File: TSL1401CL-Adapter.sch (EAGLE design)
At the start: 3 parts

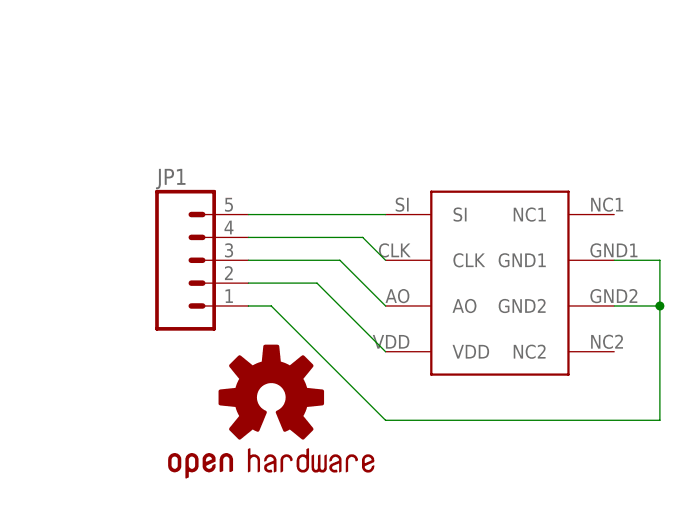
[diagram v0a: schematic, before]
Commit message: Added 2x3 Shroud and made the board square with drill holes
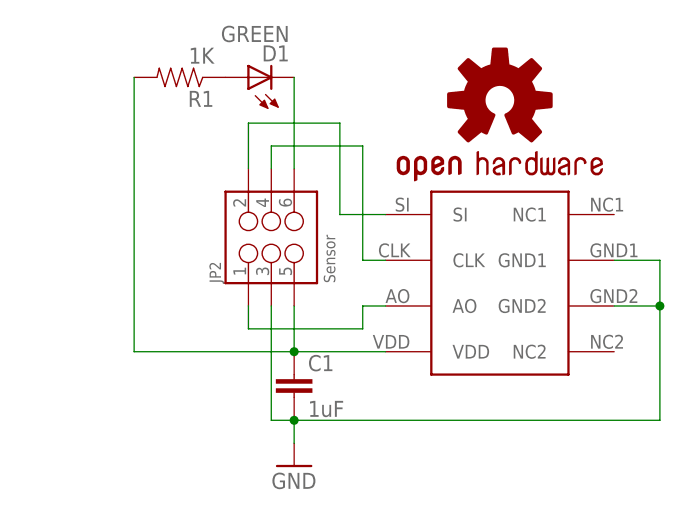
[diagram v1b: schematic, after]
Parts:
- removed JP1: (no value), SparkFun:M05LOCK_LONGPADS
- added C1: 1uF, SparkFun-Passives:CAP0603-CAP
- added D1: GREEN, SparkFun-LED:LED-GREEN0603
- added JP2: Sensor, SparkFun-Connectors:M03X2
- added R1: 1K, SparkFun-Resistors:RESISTOR0603-RES
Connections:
- new net GND: C1.2, JP2.3, U$1.GND1, U$1.GND2
- new net N$6: D1.C, JP2.6
- net N$1: now also JP2.2; no longer JP1.5
- net N$2: now also JP2.4; no longer JP1.4
- net N$3: now also JP2.1; no longer JP1.3
- net N$4: now also C1.1, JP2.5, R1.2; no longer JP1.2
- net N$5: now also D1.A, R1.1; no longer JP1.1, U$1.GND1, U$1.GND2
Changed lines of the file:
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@@
 <layer number="144" name="Drill_legend" color="7" fill="1" visible="no" active="yes"/>
 <layer number="151" name="HeatSink" color="7" fill="1" visible="no" active="yes"/>
+<layer number="199" name="Contour" color="7" fill="1" visible="yes" active="yes"/>
 <layer number="200" name="200bmp" color="1" fill="10" visible="no" active="yes"/>
 <layer number="201" name="201bmp" color="2" fill="10" visible="no" active="yes"/>
@@
 <parts>
 <part name="U$1" library="BIG" deviceset="TSL1401" device="CL"/>
-<part name="JP1" library="SparkFun" deviceset="M05" device="LOCK_LONGPADS"/>
 <part name="U$2" library="SparkFun" deviceset="OSHW-LOGO" device="M"/>
+<part name="JP2" library="SparkFun-Connectors" deviceset="M03X2" device="" value="Sensor"/>
+<part name="C1" library="SparkFun-Passives" deviceset="CAP" device="0603-CAP" value="1uF"/>
+<part name="GND1" library="SparkFun-Aesthetics" deviceset="GND" device=""/>
+<part name="R1" library="SparkFun-Resistors" deviceset="RESISTOR" device="0603-RES" value="1K"/>
+<part name="D1" library="SparkFun-LED" deviceset="LED-GREEN" device="0603" value="GREEN"/>
 </parts>
 <sheets>
@@
 <instances>
 <instance part="U$1" gate="G$1" x="78.74" y="50.8"/>
-<instance part="JP1" gate="G$1" x="43.18" y="53.34"/>
-<instance part="U$2" gate="G$1" x="53.34" y="38.1"/>
+<instance part="U$2" gate="G$1" x="78.74" y="71.12"/>
+<instance part="JP2" gate="G$1" x="53.34" y="55.88" smashed="yes" rot="R90">
+<attribute name="NAME" x="47.752" y="50.8" size="1.27" layer="95" rot="R90"/>
+<attribute name="VALUE" x="60.452" y="50.8" size="1.27" layer="96" rot="R90"/>
+</instance>
+<instance part="C1" gate="G$1" x="55.88" y="38.1"/>
+<instance part="GND1" gate="1" x="55.88" y="30.48"/>
+<instance part="R1" gate="G$1" x="43.18" y="73.66" rot="R180"/>
+<instance part="D1" gate="G$1" x="50.8" y="73.66" rot="R90"/>
 </instances>
 <busses>
@@
 <net name="N$1" class="0">
 <segment>
-<wire x1="66.04" y1="58.42" x2="50.8" y2="58.42" width="0.1524" layer="91"/>
+<wire x1="66.04" y1="58.42" x2="60.96" y2="58.42" width="0.1524" layer="91"/>
 <pinref part="U$1" gate="G$1" pin="SI"/>
-<pinref part="JP1" gate="G$1" pin="5"/>
+<wire x1="60.96" y1="58.42" x2="60.96" y2="68.58" width="0.1524" layer="91"/>
+<wire x1="60.96" y1="68.58" x2="50.8" y2="68.58" width="0.1524" layer="91"/>
+<pinref part="JP2" gate="G$1" pin="2"/>
+<wire x1="50.8" y1="68.58" x2="50.8" y2="63.5" width="0.1524" layer="91"/>
 </segment>
 </net>
 <net name="N$2" class="0">
 <segment>
-<wire x1="66.04" y1="53.34" x2="63.5" y2="55.88" width="0.1524" layer="91"/>
-<wire x1="63.5" y1="55.88" x2="50.8" y2="55.88" width="0.1524" layer="91"/>
+<wire x1="66.04" y1="53.34" x2="63.5" y2="53.34" width="0.1524" layer="91"/>
+<wire x1="63.5" y1="53.34" x2="63.5" y2="66.04" width="0.1524" layer="91"/>
 <pinref part="U$1" gate="G$1" pin="CLK"/>
-<pinref part="JP1" gate="G$1" pin="4"/>
+<wire x1="63.5" y1="66.04" x2="53.34" y2="66.04" width="0.1524" layer="91"/>
+<pinref part="JP2" gate="G$1" pin="4"/>
+<wire x1="53.34" y1="66.04" x2="53.34" y2="63.5" width="0.1524" layer="91"/>
 </segment>
 </net>
 <net name="N$3" class="0">
 <segment>
-<wire x1="66.04" y1="48.26" x2="60.96" y2="53.34" width="0.1524" layer="91"/>
-<wire x1="60.96" y1="53.34" x2="50.8" y2="53.34" width="0.1524" layer="91"/>
+<wire x1="66.04" y1="48.26" x2="63.5" y2="48.26" width="0.1524" layer="91"/>
+<wire x1="63.5" y1="48.26" x2="63.5" y2="45.72" width="0.1524" layer="91"/>
+<wire x1="63.5" y1="45.72" x2="50.8" y2="45.72" width="0.1524" layer="91"/>
+<wire x1="50.8" y1="45.72" x2="50.8" y2="48.26" width="0.1524" layer="91"/>
 <pinref part="U$1" gate="G$1" pin="AO"/>
-<pinref part="JP1" gate="G$1" pin="3"/>
+<pinref part="JP2" gate="G$1" pin="1"/>
 </segment>
 </net>
 <net name="N$4" class="0">
 <segment>
-<wire x1="66.04" y1="43.18" x2="58.42" y2="50.8" width="0.1524" layer="91"/>
-<wire x1="58.42" y1="50.8" x2="50.8" y2="50.8" width="0.1524" layer="91"/>
+<wire x1="66.04" y1="43.18" x2="55.88" y2="43.18" width="0.1524" layer="91"/>
+<wire x1="55.88" y1="43.18" x2="55.88" y2="48.26" width="0.1524" layer="91"/>
 <pinref part="U$1" gate="G$1" pin="VDD"/>
-<pinref part="JP1" gate="G$1" pin="2"/>
+<pinref part="JP2" gate="G$1" pin="5"/>
+<pinref part="C1" gate="G$1" pin="1"/>
+<junction x="55.88" y="43.18"/>
+<wire x1="55.88" y1="43.18" x2="38.1" y2="43.18" width="0.1524" layer="91"/>
+<wire x1="38.1" y1="43.18" x2="38.1" y2="73.66" width="0.1524" layer="91"/>
+<pinref part="R1" gate="G$1" pin="2"/>
+</segment>
+</net>
+<net name="GND" class="0">
+<segment>
+<pinref part="C1" gate="G$1" pin="2"/>
+<pinref part="GND1" gate="1" pin="GND"/>
+<wire x1="55.88" y1="33.02" x2="55.88" y2="35.56" width="0.1524" layer="91"/>
+<pinref part="U$1" gate="G$1" pin="GND1"/>
+<wire x1="91.44" y1="53.34" x2="96.52" y2="53.34" width="0.1524" layer="91"/>
+<wire x1="96.52" y1="53.34" x2="96.52" y2="48.26" width="0.1524" layer="91"/>
+<wire x1="91.44" y1="48.26" x2="96.52" y2="48.26" width="0.1524" layer="91"/>
+<pinref part="U$1" gate="G$1" pin="GND2"/>
+<wire x1="96.52" y1="48.26" x2="96.52" y2="35.56" width="0.1524" layer="91"/>
+<junction x="96.52" y="48.26"/>
+<wire x1="53.34" y1="35.56" x2="53.34" y2="48.26" width="0.1524" layer="91"/>
+<pinref part="JP2" gate="G$1" pin="3"/>
+<wire x1="96.52" y1="35.56" x2="55.88" y2="35.56" width="0.1524" layer="91"/>
+<junction x="55.88" y="35.56"/>
+<wire x1="55.88" y1="35.56" x2="53.34" y2="35.56" width="0.1524" layer="91"/>
 </segment>
 </net>
 <net name="N$5" class="0">
 <segment>
-<wire x1="91.44" y1="53.34" x2="96.52" y2="53.34" width="0.1524" layer="91"/>
-<wire x1="96.52" y1="53.34" x2="96.52" y2="48.26" width="0.1524" layer="91"/>
-<wire x1="96.52" y1="48.26" x2="96.52" y2="35.56" width="0.1524" layer="91"/>
-<wire x1="96.52" y1="35.56" x2="66.04" y2="35.56" width="0.1524" layer="91"/>
-<wire x1="66.04" y1="35.56" x2="53.34" y2="48.26" width="0.1524" layer="91"/>
-<wire x1="53.34" y1="48.26" x2="50.8" y2="48.26" width="0.1524" layer="91"/>
-<wire x1="91.44" y1="48.26" x2="96.52" y2="48.26" width="0.1524" layer="91"/>
-<junction x="96.52" y="48.26"/>
-<pinref part="U$1" gate="G$1" pin="GND1"/>
-<pinref part="JP1" gate="G$1" pin="1"/>
-<pinref part="U$1" gate="G$1" pin="GND2"/>
+<pinref part="R1" gate="G$1" pin="1"/>
+<pinref part="D1" gate="G$1" pin="A"/>
 </segment>
 </net>
+<net name="N$6" class="0">
+<segment>
+<pinref part="D1" gate="G$1" pin="C"/>
+<pinref part="JP2" gate="G$1" pin="6"/>
+<wire x1="55.88" y1="73.66" x2="55.88" y2="63.5" width="0.1524" layer="91"/>
+</segment>
+</net>

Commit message: Modified to be used as a remote sensor to the pgFocus project
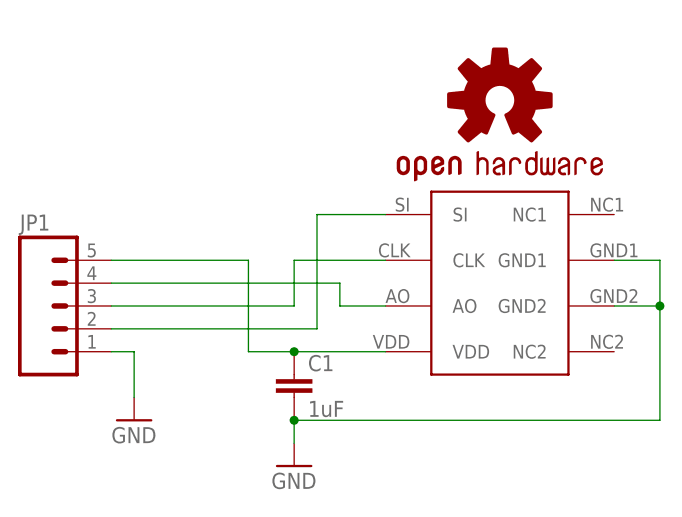
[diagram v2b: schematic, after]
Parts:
- removed D1: GREEN, SparkFun-LED:LED-GREEN0603
- removed JP2: Sensor, SparkFun-Connectors:M03X2
- removed R1: 1K, SparkFun-Resistors:RESISTOR0603-RES
- added JP1: (no value), SparkFun-Connectors:M05LOCK
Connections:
- removed net N$1: JP2.2, U$1.SI
- removed net N$2: JP2.4, U$1.CLK
- removed net N$3: JP2.1, U$1.AO
- removed net N$4: C1.1, JP2.5, R1.2, U$1.VDD
- removed net N$5: D1.A, R1.1
- removed net N$6: D1.C, JP2.6
- new net +5V: C1.1, JP1.5, U$1.VDD
- new net AO: JP1.4, U$1.AO
- new net CLK: JP1.3, U$1.CLK
- new net SI: JP1.2, U$1.SI
- net GND: now also JP1.1; no longer JP2.3
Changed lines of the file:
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@@
 <part name="U$1" library="BIG" deviceset="TSL1401" device="CL"/>
 <part name="U$2" library="SparkFun" deviceset="OSHW-LOGO" device="M"/>
-<part name="JP2" library="SparkFun-Connectors" deviceset="M03X2" device="" value="Sensor"/>
 <part name="C1" library="SparkFun-Passives" deviceset="CAP" device="0603-CAP" value="1uF"/>
 <part name="GND1" library="SparkFun-Aesthetics" deviceset="GND" device=""/>
-<part name="R1" library="SparkFun-Resistors" deviceset="RESISTOR" device="0603-RES" value="1K"/>
-<part name="D1" library="SparkFun-LED" deviceset="LED-GREEN" device="0603" value="GREEN"/>
+<part name="JP1" library="SparkFun-Connectors" deviceset="M05" device="LOCK"/>
+<part name="GND2" library="SparkFun-Aesthetics" deviceset="GND" device=""/>
 </parts>
 <sheets>
@@
 <instance part="U$1" gate="G$1" x="78.74" y="50.8"/>
 <instance part="U$2" gate="G$1" x="78.74" y="71.12"/>
-<instance part="JP2" gate="G$1" x="53.34" y="55.88" smashed="yes" rot="R90">
-<attribute name="NAME" x="47.752" y="50.8" size="1.27" layer="95" rot="R90"/>
-<attribute name="VALUE" x="60.452" y="50.8" size="1.27" layer="96" rot="R90"/>
-</instance>
 <instance part="C1" gate="G$1" x="55.88" y="38.1"/>
 <instance part="GND1" gate="1" x="55.88" y="30.48"/>
-<instance part="R1" gate="G$1" x="43.18" y="73.66" rot="R180"/>
-<instance part="D1" gate="G$1" x="50.8" y="73.66" rot="R90"/>
+<instance part="JP1" gate="G$1" x="27.94" y="48.26"/>
+<instance part="GND2" gate="1" x="38.1" y="35.56"/>
 </instances>
 <busses>
 </busses>
 <nets>
-<net name="N$1" class="0">
-<segment>
-<wire x1="66.04" y1="58.42" x2="60.96" y2="58.42" width="0.1524" layer="91"/>
-<pinref part="U$1" gate="G$1" pin="SI"/>
-<wire x1="60.96" y1="58.42" x2="60.96" y2="68.58" width="0.1524" layer="91"/>
-<wire x1="60.96" y1="68.58" x2="50.8" y2="68.58" width="0.1524" layer="91"/>
-<pinref part="JP2" gate="G$1" pin="2"/>
-<wire x1="50.8" y1="68.58" x2="50.8" y2="63.5" width="0.1524" layer="91"/>
-</segment>
-</net>
-<net name="N$2" class="0">
-<segment>
-<wire x1="66.04" y1="53.34" x2="63.5" y2="53.34" width="0.1524" layer="91"/>
-<wire x1="63.5" y1="53.34" x2="63.5" y2="66.04" width="0.1524" layer="91"/>
-<pinref part="U$1" gate="G$1" pin="CLK"/>
-<wire x1="63.5" y1="66.04" x2="53.34" y2="66.04" width="0.1524" layer="91"/>
-<pinref part="JP2" gate="G$1" pin="4"/>
-<wire x1="53.34" y1="66.04" x2="53.34" y2="63.5" width="0.1524" layer="91"/>
-</segment>
-</net>
-<net name="N$3" class="0">
-<segment>
-<wire x1="66.04" y1="48.26" x2="63.5" y2="48.26" width="0.1524" layer="91"/>
-<wire x1="63.5" y1="48.26" x2="63.5" y2="45.72" width="0.1524" layer="91"/>
-<wire x1="63.5" y1="45.72" x2="50.8" y2="45.72" width="0.1524" layer="91"/>
-<wire x1="50.8" y1="45.72" x2="50.8" y2="48.26" width="0.1524" layer="91"/>
-<pinref part="U$1" gate="G$1" pin="AO"/>
-<pinref part="JP2" gate="G$1" pin="1"/>
-</segment>
-</net>
-<net name="N$4" class="0">
+<net name="+5V" class="0">
 <segment>
 <wire x1="66.04" y1="43.18" x2="55.88" y2="43.18" width="0.1524" layer="91"/>
-<wire x1="55.88" y1="43.18" x2="55.88" y2="48.26" width="0.1524" layer="91"/>
 <pinref part="U$1" gate="G$1" pin="VDD"/>
-<pinref part="JP2" gate="G$1" pin="5"/>
 <pinref part="C1" gate="G$1" pin="1"/>
+<wire x1="55.88" y1="43.18" x2="50.8" y2="43.18" width="0.1524" layer="91"/>
 <junction x="55.88" y="43.18"/>
-<wire x1="55.88" y1="43.18" x2="38.1" y2="43.18" width="0.1524" layer="91"/>
-<wire x1="38.1" y1="43.18" x2="38.1" y2="73.66" width="0.1524" layer="91"/>
-<pinref part="R1" gate="G$1" pin="2"/>
+<wire x1="50.8" y1="43.18" x2="50.8" y2="53.34" width="0.1524" layer="91"/>
+<pinref part="JP1" gate="G$1" pin="5"/>
+<wire x1="50.8" y1="53.34" x2="35.56" y2="53.34" width="0.1524" layer="91"/>
 </segment>
 </net>
@@
 <wire x1="96.52" y1="48.26" x2="96.52" y2="35.56" width="0.1524" layer="91"/>
 <junction x="96.52" y="48.26"/>
-<wire x1="53.34" y1="35.56" x2="53.34" y2="48.26" width="0.1524" layer="91"/>
-<pinref part="JP2" gate="G$1" pin="3"/>
 <wire x1="96.52" y1="35.56" x2="55.88" y2="35.56" width="0.1524" layer="91"/>
 <junction x="55.88" y="35.56"/>
-<wire x1="55.88" y1="35.56" x2="53.34" y2="35.56" width="0.1524" layer="91"/>
+</segment>
+<segment>
+<pinref part="GND2" gate="1" pin="GND"/>
+<wire x1="38.1" y1="38.1" x2="38.1" y2="43.18" width="0.1524" layer="91"/>
+<pinref part="JP1" gate="G$1" pin="1"/>
+<wire x1="38.1" y1="43.18" x2="35.56" y2="43.18" width="0.1524" layer="91"/>
 </segment>
 </net>
-<net name="N$5" class="0">
+<net name="SI" class="0">
 <segment>
-<pinref part="R1" gate="G$1" pin="1"/>
-<pinref part="D1" gate="G$1" pin="A"/>
+<pinref part="U$1" gate="G$1" pin="SI"/>
+<wire x1="66.04" y1="58.42" x2="58.42" y2="58.42" width="0.1524" layer="91"/>
+<wire x1="58.42" y1="58.42" x2="58.42" y2="45.72" width="0.1524" layer="91"/>
+<pinref part="JP1" gate="G$1" pin="2"/>
+<wire x1="58.42" y1="45.72" x2="35.56" y2="45.72" width="0.1524" layer="91"/>
 </segment>
 </net>
-<net name="N$6" class="0">
+<net name="AO" class="0">
 <segment>
-<pinref part="D1" gate="G$1" pin="C"/>
-<pinref part="JP2" gate="G$1" pin="6"/>
-<wire x1="55.88" y1="73.66" x2="55.88" y2="63.5" width="0.1524" layer="91"/>
+<pinref part="U$1" gate="G$1" pin="AO"/>
+<wire x1="66.04" y1="48.26" x2="60.96" y2="48.26" width="0.1524" layer="91"/>
+<wire x1="60.96" y1="48.26" x2="60.96" y2="50.8" width="0.1524" layer="91"/>
+<pinref part="JP1" gate="G$1" pin="4"/>
+<wire x1="60.96" y1="50.8" x2="35.56" y2="50.8" width="0.1524" layer="91"/>
 </segment>
 </net>
+<net name="CLK" class="0">
+<segment>
+<pinref part="U$1" gate="G$1" pin="CLK"/>
+<wire x1="66.04" y1="53.34" x2="55.88" y2="53.34" width="0.1524" layer="91"/>
+<wire x1="55.88" y1="53.34" x2="55.88" y2="48.26" width="0.1524" layer="91"/>
+<pinref part="JP1" gate="G$1" pin="3"/>
+<wire x1="55.88" y1="48.26" x2="35.56" y2="48.26" width="0.1524" layer="91"/>
+</segment>
+</net>

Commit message: Changed connector to JST 5 Pin
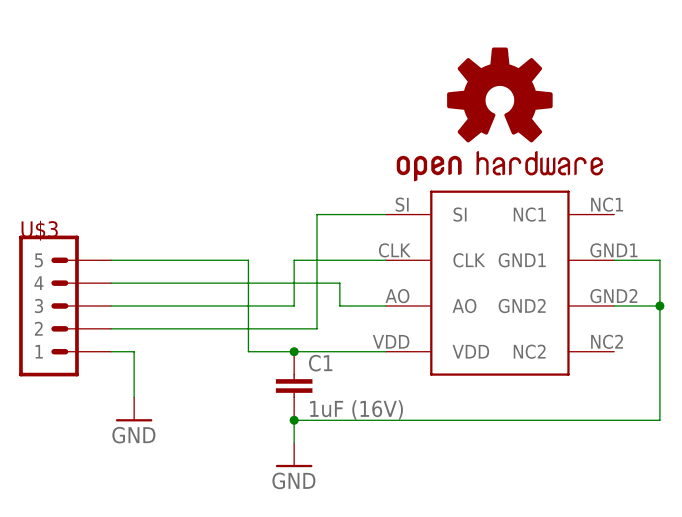
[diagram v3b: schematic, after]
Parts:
- removed JP1: (no value), SparkFun-Connectors:M05LOCK
- added U$3: M05, BIG:M05
- C1: value 1uF -> 1uF (16V)
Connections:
- net +5V: now also U$3.5; no longer JP1.5
- net AO: now also U$3.4; no longer JP1.4
- net CLK: now also U$3.3; no longer JP1.3
- net GND: now also U$3.1; no longer JP1.1
- net SI: now also U$3.2; no longer JP1.2
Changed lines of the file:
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@@
 <part name="U$1" library="BIG" deviceset="TSL1401" device="CL"/>
 <part name="U$2" library="SparkFun" deviceset="OSHW-LOGO" device="M"/>
-<part name="C1" library="SparkFun-Passives" deviceset="CAP" device="0603-CAP" value="1uF"/>
+<part name="C1" library="SparkFun-Passives" deviceset="CAP" device="0603-CAP" value="1uF (16V)"/>
 <part name="GND1" library="SparkFun-Aesthetics" deviceset="GND" device=""/>
-<part name="JP1" library="SparkFun-Connectors" deviceset="M05" device="LOCK"/>
 <part name="GND2" library="SparkFun-Aesthetics" deviceset="GND" device=""/>
+<part name="U$3" library="BIG" deviceset="M05" device=""/>
 </parts>
 <sheets>
@@
 <instance part="C1" gate="G$1" x="55.88" y="38.1"/>
 <instance part="GND1" gate="1" x="55.88" y="30.48"/>
-<instance part="JP1" gate="G$1" x="27.94" y="48.26"/>
 <instance part="GND2" gate="1" x="38.1" y="35.56"/>
+<instance part="U$3" gate="G$1" x="30.48" y="48.26"/>
 </instances>
 <busses>
@@
 <junction x="55.88" y="43.18"/>
 <wire x1="50.8" y1="43.18" x2="50.8" y2="53.34" width="0.1524" layer="91"/>
-<pinref part="JP1" gate="G$1" pin="5"/>
 <wire x1="50.8" y1="53.34" x2="35.56" y2="53.34" width="0.1524" layer="91"/>
+<pinref part="U$3" gate="G$1" pin="5"/>
 </segment>
 </net>
@@
 <pinref part="GND2" gate="1" pin="GND"/>
 <wire x1="38.1" y1="38.1" x2="38.1" y2="43.18" width="0.1524" layer="91"/>
-<pinref part="JP1" gate="G$1" pin="1"/>
 <wire x1="38.1" y1="43.18" x2="35.56" y2="43.18" width="0.1524" layer="91"/>
+<pinref part="U$3" gate="G$1" pin="1"/>
 </segment>
 </net>
@@
 <wire x1="66.04" y1="58.42" x2="58.42" y2="58.42" width="0.1524" layer="91"/>
 <wire x1="58.42" y1="58.42" x2="58.42" y2="45.72" width="0.1524" layer="91"/>
-<pinref part="JP1" gate="G$1" pin="2"/>
 <wire x1="58.42" y1="45.72" x2="35.56" y2="45.72" width="0.1524" layer="91"/>
+<pinref part="U$3" gate="G$1" pin="2"/>
 </segment>
 </net>
@@
 <wire x1="66.04" y1="48.26" x2="60.96" y2="48.26" width="0.1524" layer="91"/>
 <wire x1="60.96" y1="48.26" x2="60.96" y2="50.8" width="0.1524" layer="91"/>
-<pinref part="JP1" gate="G$1" pin="4"/>
 <wire x1="60.96" y1="50.8" x2="35.56" y2="50.8" width="0.1524" layer="91"/>
+<pinref part="U$3" gate="G$1" pin="4"/>
 </segment>
 </net>
@@
 <wire x1="66.04" y1="53.34" x2="55.88" y2="53.34" width="0.1524" layer="91"/>
 <wire x1="55.88" y1="53.34" x2="55.88" y2="48.26" width="0.1524" layer="91"/>
-<pinref part="JP1" gate="G$1" pin="3"/>
 <wire x1="55.88" y1="48.26" x2="35.56" y2="48.26" width="0.1524" layer="91"/>
+<pinref part="U$3" gate="G$1" pin="3"/>
 </segment>
 </net>
